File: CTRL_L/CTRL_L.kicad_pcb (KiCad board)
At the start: 2 copper layers, 34 x 63.9 mm, 24 parts, among them J1 BM14B-NSHSS-TBT_LF__SN_, J2 BM04B-NSHSS-TBT_LF__SN_, J3 BM04B-NSHSS-TBT_LF__SN_, J4 5051100592, U1 74LVC1G08

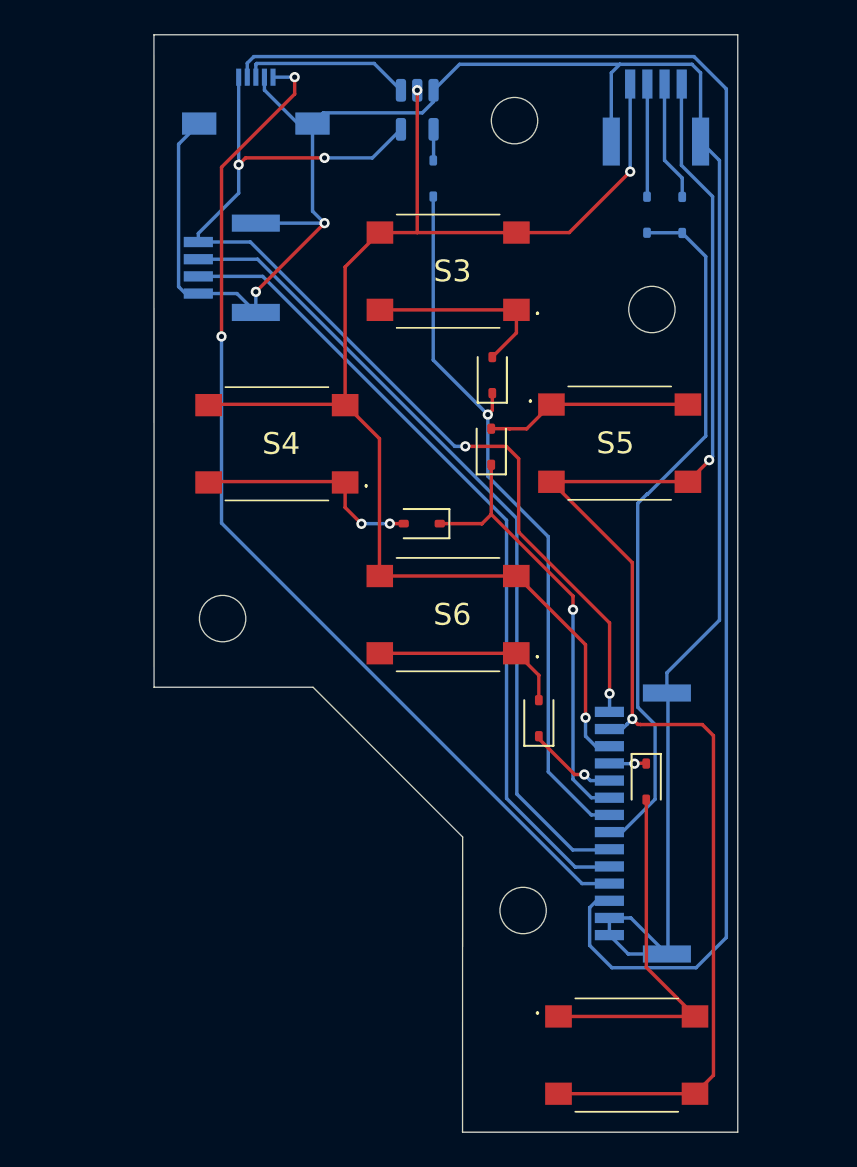
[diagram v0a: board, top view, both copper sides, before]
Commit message: CTRL_L Cleanup: Reduced 14 to 12 pins, added Ground Planes and Vias, and general wiring cleanups
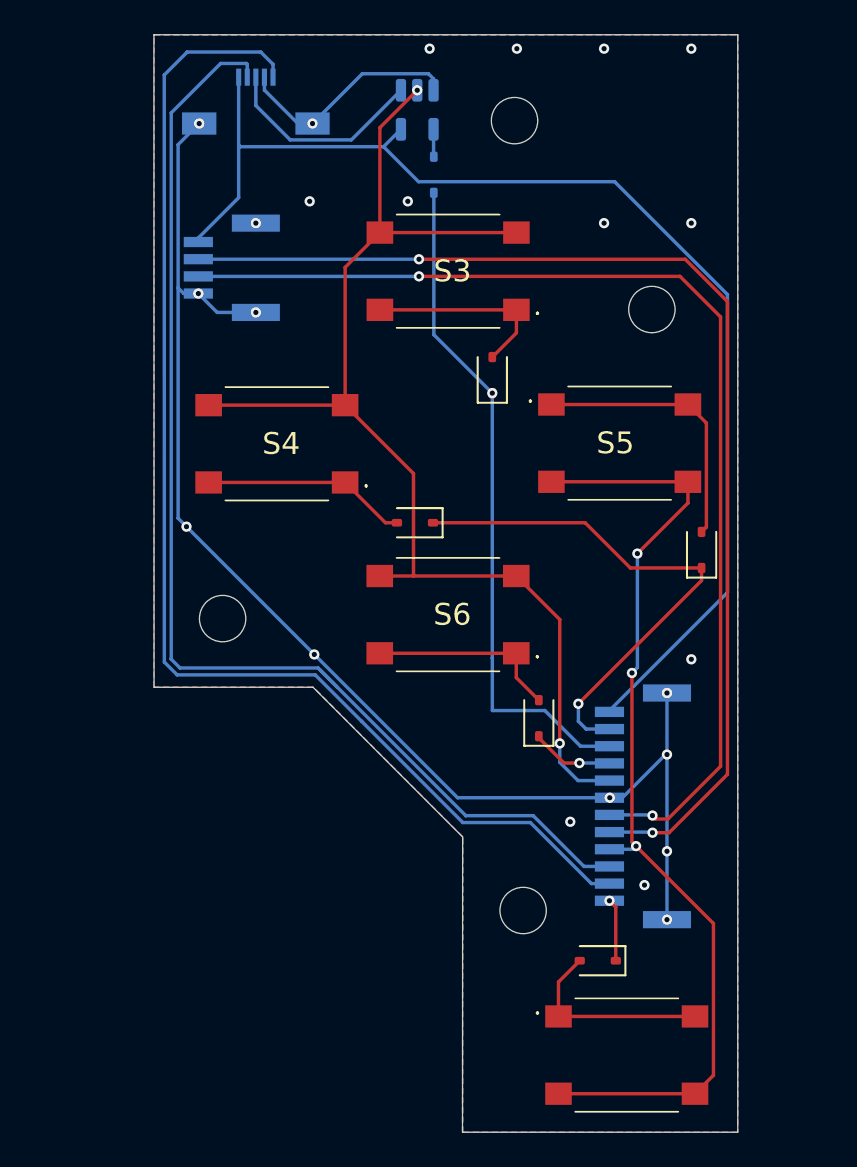
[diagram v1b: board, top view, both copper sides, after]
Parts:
- removed D1, D2: 1N4148WS, Diode_SMD:D_SOD-323
- removed J1: BM14B-NSHSS-TBT_LF__SN_, BM14B-NSHSS-TBT:BM14BNSHSSTBTLFSN
- J2: value BM04B-NSHSS-TBT_LF__SN_ -> BM12B-NSHSS-TBT_LF__SN_; footprint BM04B-NSHSS-TBT:BM04BNSHSSTBTLFSN -> BM12B-NSHSS-TBT_LF__SN_:BM12BNSHSSTBTLFSN
- moved J2 39.8 mm to (160.0, 110.2), turned to -90 degrees
- moved D5 13.6 mm to (163.2, 95.2)
- moved D7 10.8 mm to (157.1, 119.2), turned to 180 degrees
- moved D4 0.40 mm to (146.5, 93.6)
- moved D8 0.22 mm to (147.6, 73.4)
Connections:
- J2 pad 1: Col1 -> Row5
- J2 pad 2: Net-(D1-A) -> /ADC_Y
- J2 pad 3: Net-(D2-A) -> /ADC_X
- J2 pad 5: GND -> SL_VOL
- J2 pad 6: GND -> SL_BRI
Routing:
- net Row1: track 40.4 -> 0.00 mm
- net GND: track 126.1 -> 91.9 mm, vias 2 -> 23
- net Col2: track 83.2 -> 56.9 mm, vias 2 -> 3
- net /ADC_X: track 91.1 -> 70.1 mm
- net SL_VOL: track 47.6 -> 67.7 mm, vias 0 -> 2
- net SL_BRI: track 47.7 -> 65.4 mm, vias 0 -> 2
- net /ADC_Y: track 60.3 -> 73.4 mm, vias 2 -> 0
- net Net-(D7-A): track 21.8 -> 11.7 mm
- net +3V3: track 61.7 -> 71.2 mm, vias 4 -> 0
- net Col1: track 79.8 -> 70.8 mm, vias 3 -> 2
- net Net-(D2-A): track 7.00 -> 0.00 mm
- net Net-(D1-A): track 6.54 -> 0.00 mm
- net Row3: track 26.1 -> 30.6 mm
- net Net-(D5-A): track 12.1 -> 15.9 mm
- net Row2: track 42.2 -> 39.2 mm
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- added copper zone on B.Cu, net GND
- added copper zone on F.Cu, net GND

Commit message: Corrected CTRL_PWR (+other WIP changes)
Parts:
- removed J2: BM12B-NSHSS-TBT_LF__SN_, BM12B-NSHSS-TBT_LF__SN_:BM12BNSHSSTBTLFSN
- added J1: 503480-0540, 503480-0540:5034800540, B.Cu at (137.2, 69.3)
- added U2: DRV5033FAxDBZ, Package_TO_SOT_SMD:SOT-23, F.Cu at (134.7, 82.7)
- J4: value 5051100592 -> BM14B-NSHSS-TBT_LF__SN_; footprint 5051100592:CON_5051100592_MOL -> BM14B-NSHSS-TBT:BM14BNSHSSTBTLFSN
- moved J4 45.1 mm to (160.0, 109.1), turned to -90 degrees
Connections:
- J4 pad 1: /ADC_Y -> Row5
- J4 pad 2: GND -> /ADC_X
- J4 pad 3: /SW -> /ADC_Y
- J4 pad 4: /ADC_X -> Col2
- J4 pad 5: +3V3 -> SL_VOL
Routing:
- net GND: track 91.9 -> 4.06 mm, vias 23 -> 14
- net HALL: track 0.00 -> 38.5 mm, vias 0 -> 1
- net +3V3: track 71.2 -> 81.2 mm, vias 0 -> 1
- net /ADC_Y: track 73.4 -> 70.1 mm
- net /ADC_X: track 70.1 -> 73.4 mm
- net Row3: track 30.6 -> 33.1 mm

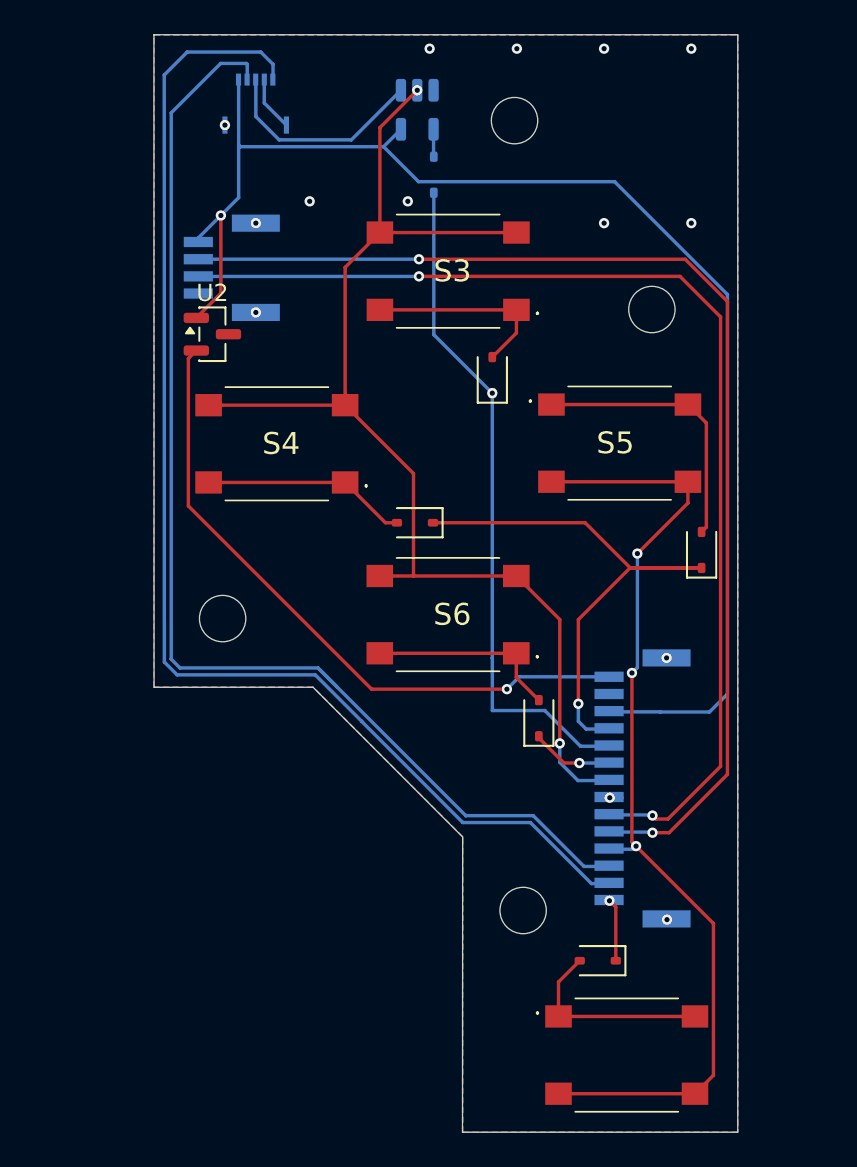
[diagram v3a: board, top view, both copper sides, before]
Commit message: Added ESD Diodes to CTRL_L.
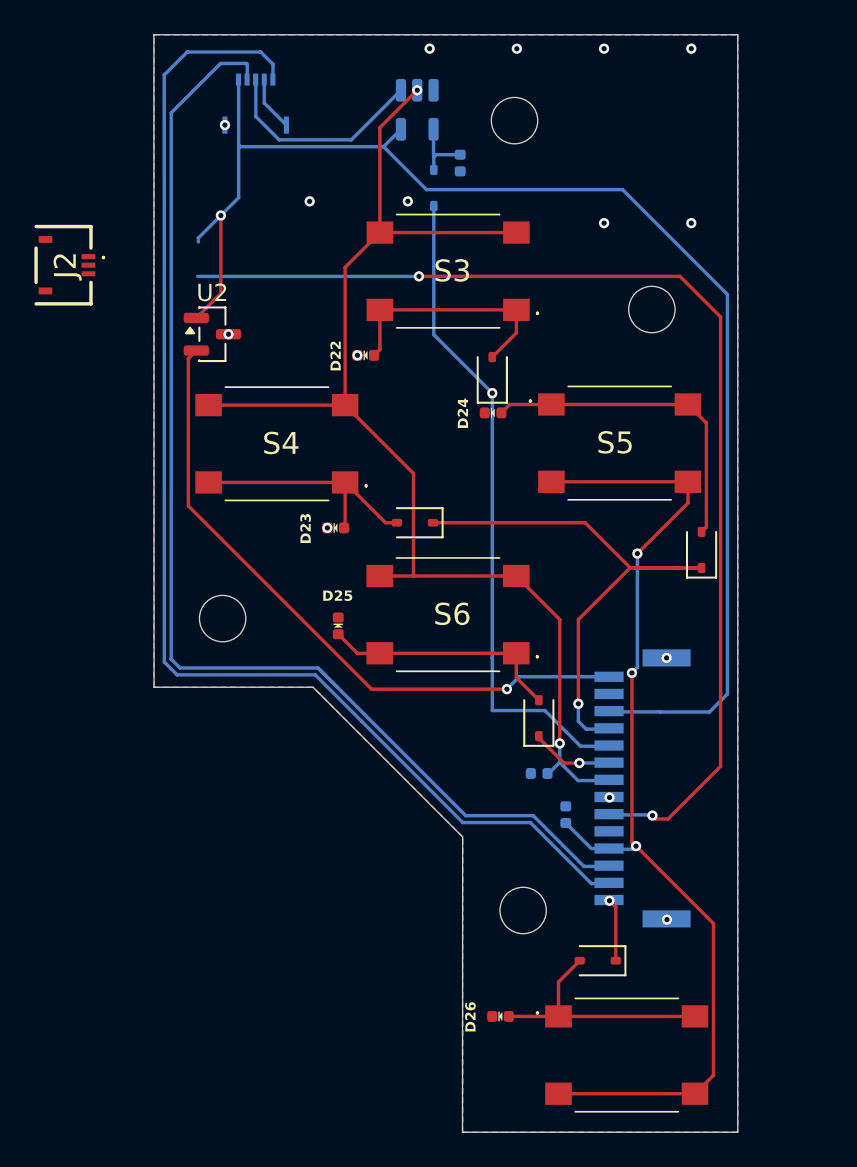
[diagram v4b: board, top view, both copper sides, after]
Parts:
- removed J3: BM04B-NSHSS-TBT_LF__SN_, BM04B-NSHSS-TBT:BM04BNSHSSTBTLFSN
- added D22: ESD5V0B03, A_HDJ_Library:D_0402_1005Metric, F.Cu at (143.6, 83.9)
- added D23: ESD5V0B03, A_HDJ_Library:D_0402_1005Metric, F.Cu at (141.8, 94.0)
- added D24: ESD5V0B03, A_HDJ_Library:D_0402_1005Metric, F.Cu at (151.0, 87.2)
- added D25: ESD5V0B03, A_HDJ_Library:D_0402_1005Metric, F.Cu at (142.0, 99.7)
- added D26: ESD5V0B03, A_HDJ_Library:D_0402_1005Metric, F.Cu at (151.4, 122.4)
- added D27: ESD5V0B03, A_HDJ_Library:D_0402_1005Metric, B.Cu at (149.1, 72.7)
- added D28: ESD5V0B03, A_HDJ_Library:D_0402_1005Metric, B.Cu at (153.7, 108.2)
- added D29: ESD5V0B03, A_HDJ_Library:D_0402_1005Metric, B.Cu at (155.2, 110.7)
- added J2: AYF530365TA, AYF530365TA:AYF530365T, F.Cu at (126.0, 78.7)
- moved D8 0.77 mm to (147.6, 74.2)
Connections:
- J4 pad 5: SL_VOL -> GND
- J4 pad 6: SL_BRI -> SL_VOL
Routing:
- net SL_BRI: track 65.4 -> 0.00 mm, vias 2 -> 0
- net Col2: track 56.9 -> 60.1 mm
- net Net-(D24-A2): track 15.9 -> 19.0 mm
- net Net-(D26-A2): track 11.7 -> 14.6 mm
- net Net-(D25-A2): track 11.2 -> 14.1 mm
- net Net-(D22-A2): track 11.3 -> 14.1 mm
- net Net-(D23-A2): track 11.9 -> 14.6 mm
- net Net-(D27-A2): track 1.60 -> 3.95 mm
- net SL_VOL: track 67.7 -> 65.4 mm
- net Col1: track 70.8 -> 71.7 mm
- net GND: track 4.06 -> 3.23 mm, vias 14 -> 15
- net Row2: track 39.2 -> 38.5 mm

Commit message: Updated CTRL_L to use FPC connectors, single volume slider, extra connector for CTRL_Z and added ESD Diodes.
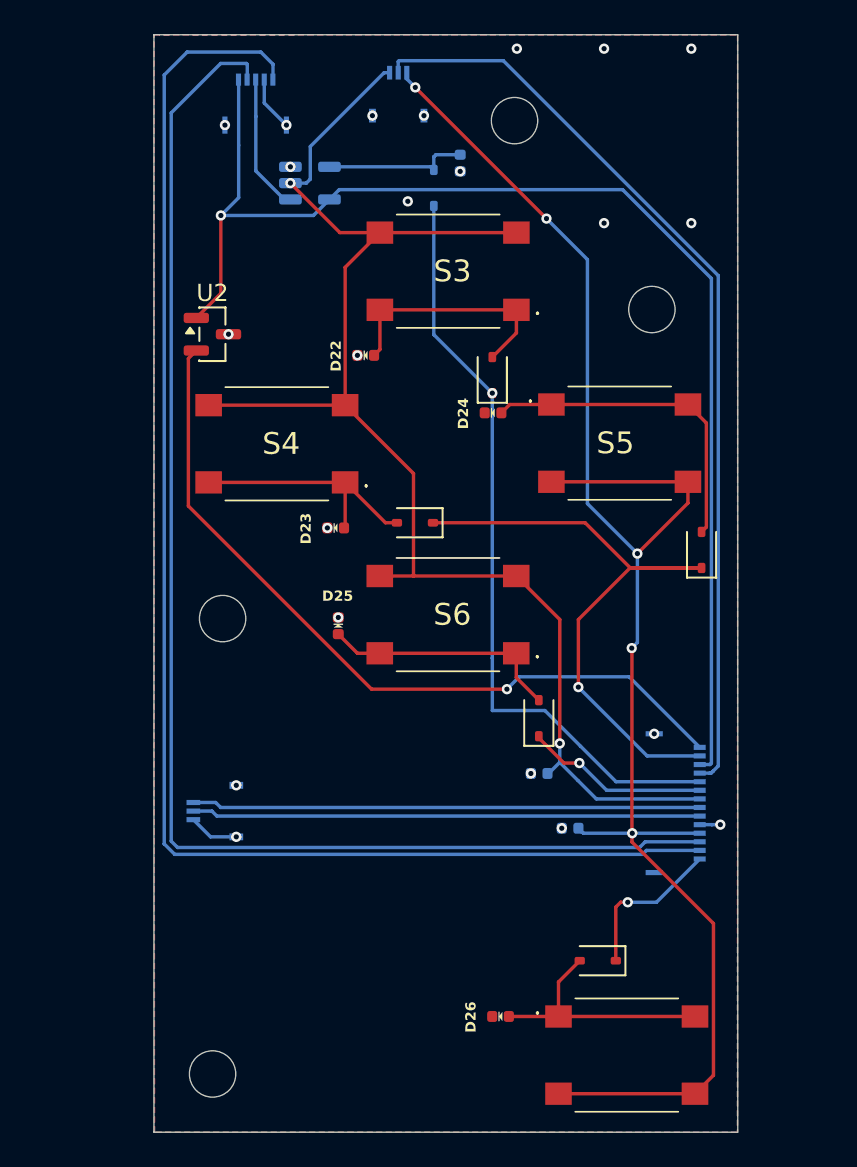
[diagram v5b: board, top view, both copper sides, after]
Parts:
- removed J4: BM14B-NSHSS-TBT_LF__SN_, BM14B-NSHSS-TBT:BM14BNSHSSTBTLFSN
- added J3: 5034801400, 5034801400:5034801400, B.Cu at (161.6, 110.0)
- added J6: AYF530365TA, AYF530365TA:AYF530365T, B.Cu at (145.5, 68.9)
- J2: moved to B.Cu
- moved J2 33.0 mm to (135.0, 110.4)
- moved H4 20.4 mm to (134.7, 125.8)
- moved U1 7.57 mm to (140.3, 73.9), turned to 0 degrees
- moved D29 0.83 mm to (155.5, 111.4), turned to 0 degrees
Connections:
- J2 pad 1: +3V3 -> SL_VIN
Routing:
- net Row1: track 0.00 -> 54.3 mm
- net Col2: track 60.1 -> 96.1 mm, vias 3 -> 5
- net SL_VOL: track 65.4 -> 29.6 mm, vias 2 -> 0
- net SL_VIN: track 0.00 -> 29.6 mm
- net Col1: track 71.7 -> 84.2 mm
- net /ADC_X: track 73.4 -> 84.2 mm
- net /ADC_Y: track 70.1 -> 79.9 mm
- net HALL: track 38.5 -> 45.4 mm
- net Row2: track 38.5 -> 44.6 mm
- net Row4: track 4.83 -> 10.7 mm
- net +3V3: track 81.2 -> 75.3 mm
- net Row5: track 3.64 -> 9.17 mm
- net Row3: track 33.1 -> 37.8 mm
- net Net-(D27-A2): track 3.95 -> 8.50 mm
- net /SW: track 12.5 -> 8.16 mm
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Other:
- outline, holes or cut-outs redrawn

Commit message: Updated CTRL_L to use 4 pin FPC (3 pin is hard to source!)
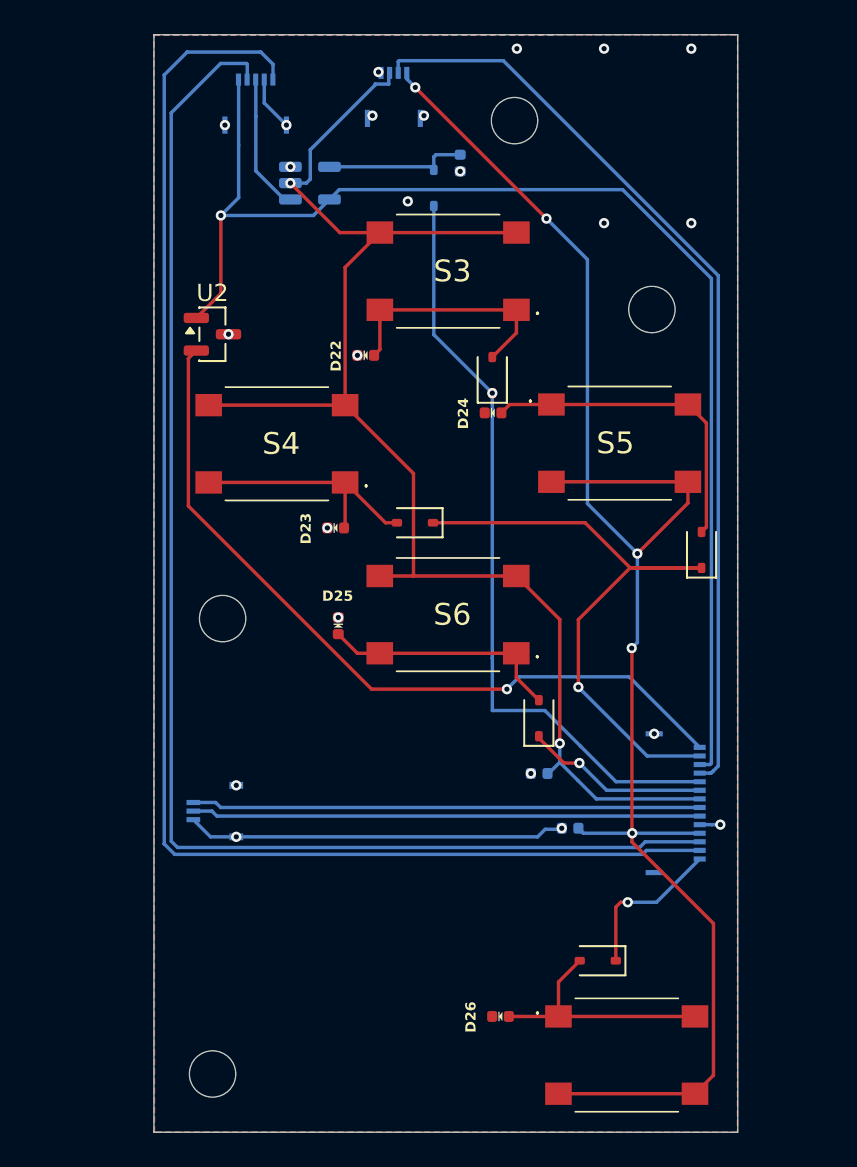
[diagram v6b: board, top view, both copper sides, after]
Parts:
- removed J6: AYF530365TA, AYF530365TA:AYF530365T
- added J4: 503480-0440, 503480-0440:5034800440, B.Cu at (145.2, 69.0)
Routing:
- net GND: track 7.30 -> 26.6 mm, vias 22 -> 23

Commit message: Updated CTRLs to be one sided (saves a billion dollars somehow), added LCSC_Parts for BOM, and other fixes. (Part 1/2)
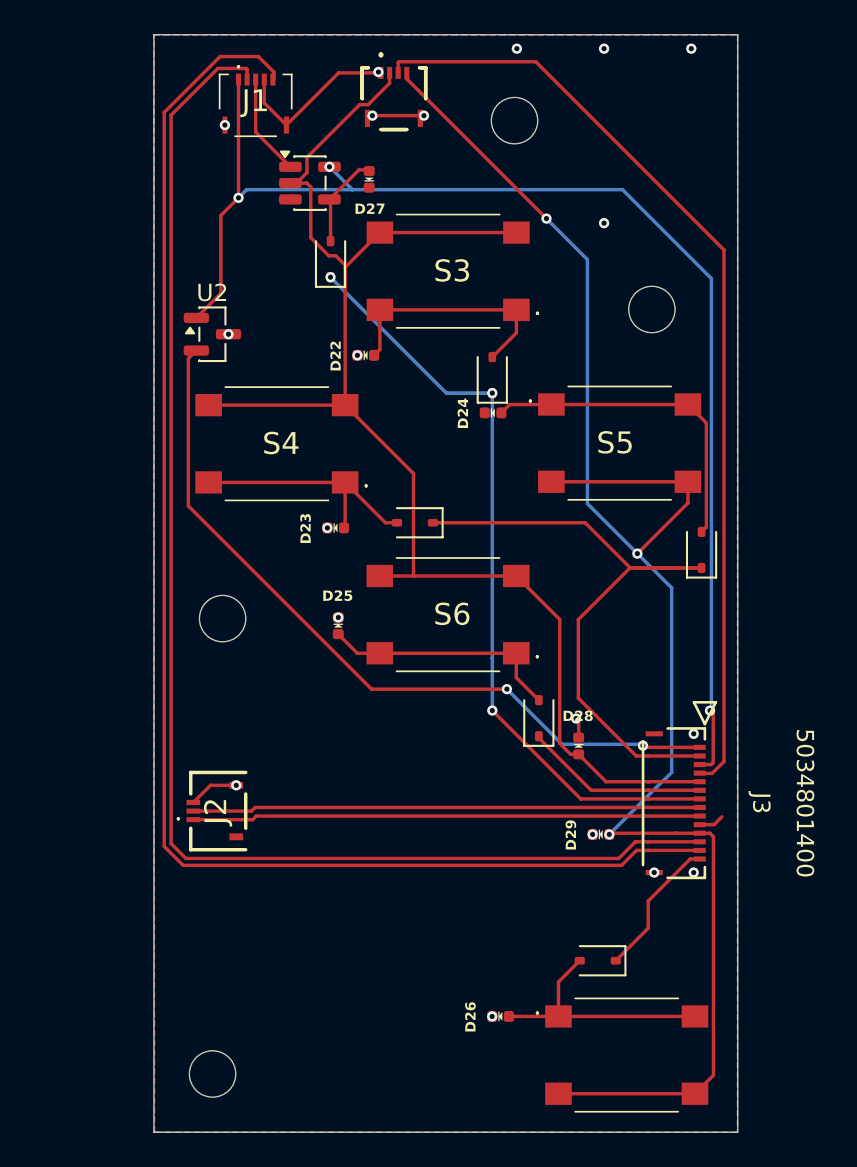
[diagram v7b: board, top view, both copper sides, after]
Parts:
- D27, D28, D29, D8, J1, J2, J3, J4, U1: moved to F.Cu
- moved D8 7.31 mm to (141.6, 78.3)
- moved D27 5.38 mm to (143.8, 73.7)
- moved D28 2.80 mm to (156.0, 106.7), turned to -90 degrees
- moved D29 1.84 mm to (157.3, 111.8)
- turned J1 to 0 degrees
- turned J2 to 90 degrees
- turned J3 to -90 degrees
- turned J4 to 0 degrees
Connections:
- J1 pad 1: /ADC_X -> +3V3
- J1 pad 2: GND -> /ADC_Y
- J1 pad 4: /ADC_Y -> GND
- J1 pad 5: +3V3 -> /ADC_X
- J3 pad 1: Row5 -> HALL
- J3 pad 10: Row2 -> GND
- J3 pad 11: Row1 -> Col2
- J3 pad 12: +3V3 -> /ADC_Y
- J3 pad 13: Row3 -> /ADC_X
- J3 pad 14: HALL -> Row5
- J3 pad 2: /ADC_X -> Row3
- J3 pad 3: /ADC_Y -> +3V3
- J3 pad 4: Col2 -> Row1
- J3 pad 5: GND -> Col1
- J3 pad 6: SL_VOL -> Row4
- J3 pad 7: SL_VIN -> Row2
- J3 pad 8: Col1 -> SL_VOL
- J3 pad 9: Row4 -> SL_VIN
- J4 pad 1: Col2 -> GND
- J4 pad 2: Row1 -> Col1
- J4 pad 3: Col1 -> Row1
- J4 pad 4: GND -> Col2
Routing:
- net GND: track 26.6 -> 18.9 mm, vias 23 -> 19
- net Net-(D27-A2): track 8.50 -> 5.51 mm
- net /SW: track 8.16 -> 5.92 mm
- net Col1: track 84.5 -> 82.5 mm, vias 2 -> 0
- net Row1: track 54.3 -> 55.4 mm
- net /ADC_X: track 84.2 -> 83.3 mm
- net Col2: track 96.1 -> 95.1 mm, vias 5 -> 3
- net Row5: track 9.17 -> 8.27 mm, vias 1 -> 0
- net HALL: track 45.4 -> 44.8 mm, vias 1 -> 2
- net +3V3: track 75.3 -> 75.8 mm, vias 1 -> 3
- net Row3: track 37.8 -> 38.2 mm, vias 1 -> 0
- net Row2: track 44.6 -> 44.9 mm, vias 1 -> 3
- net Row4: vias 1 -> 0
